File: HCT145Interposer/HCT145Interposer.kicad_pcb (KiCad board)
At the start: 2 copper layers, 33 x 40.6 mm, 8 parts, among them J1 Conn_01x01, J3 Header, J7 FORWARD, J8 REVERSE, U1 74HCT125, U2 74LVC245

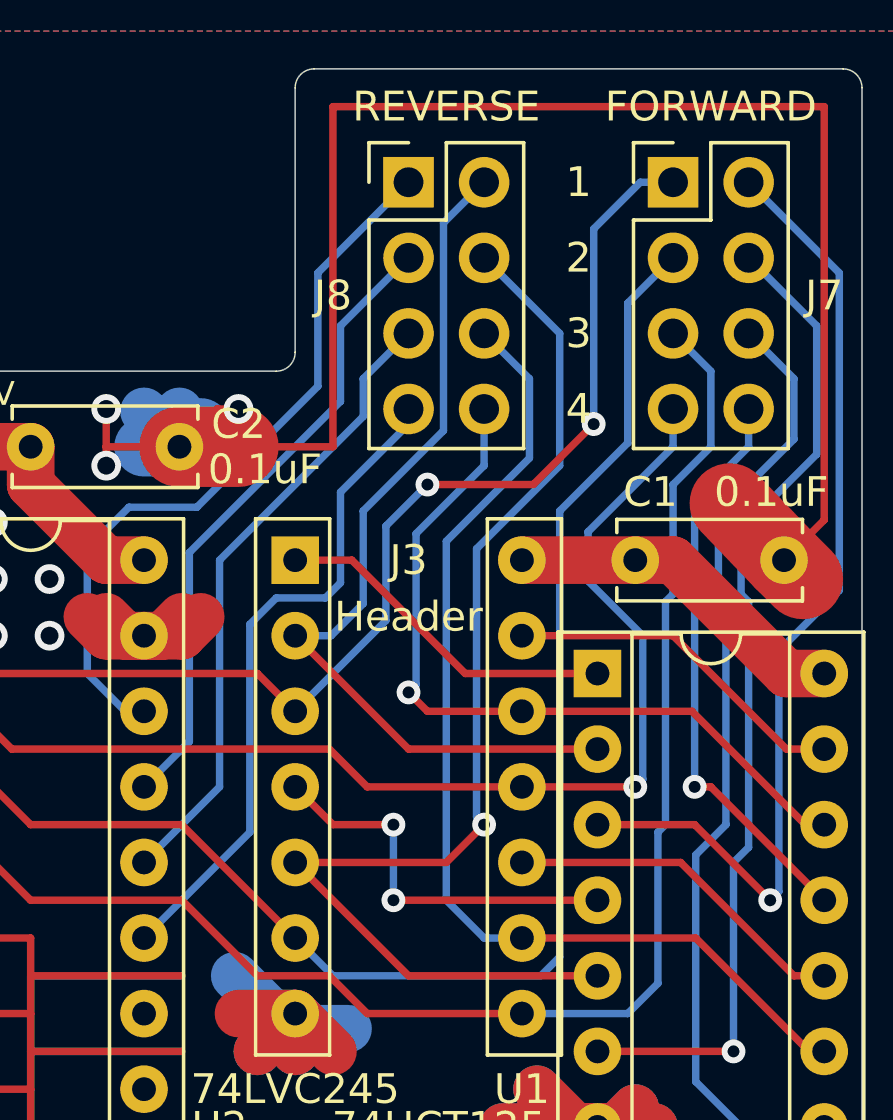
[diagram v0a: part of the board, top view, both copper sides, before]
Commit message: Quick fix to HCT145 interposer. Reverse direction was outputting to wrong pins.
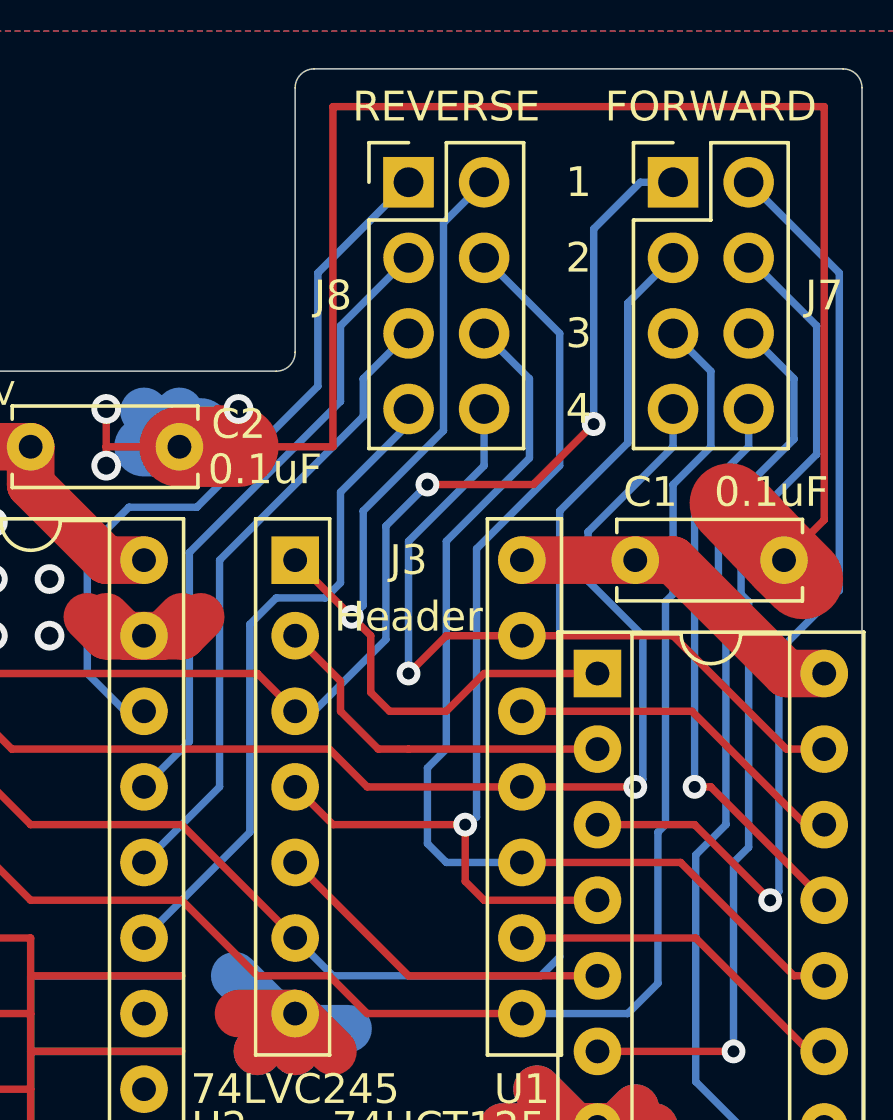
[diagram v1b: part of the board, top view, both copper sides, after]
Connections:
- J8 pad 2: GATE0_IN -> GATE0_~OE
- J8 pad 4: GATE1_IN -> GATE1_~OE
- J8 pad 6: GATE2_IN -> GATE2_~OE
- J8 pad 8: GATE3_IN -> GATE3_~OE
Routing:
- net GATE1_IN: track 40.0 -> 11.7 mm, vias 1 -> 0
- net GATE2_IN: track 35.6 -> 11.7 mm
- net GATE2_~OE: track 11.7 -> 34.4 mm
- net GATE1_~OE: track 13.2 -> 34.3 mm, vias 2 -> 1
- net GATE0_~OE: track 11.7 -> 30.4 mm, vias 0 -> 1
- net GATE0_IN: track 30.3 -> 12.3 mm
- net GATE3_IN: track 26.4 -> 11.7 mm, vias 1 -> 0
- net GATE3_~OE: track 11.7 -> 26.0 mm, vias 0 -> 1

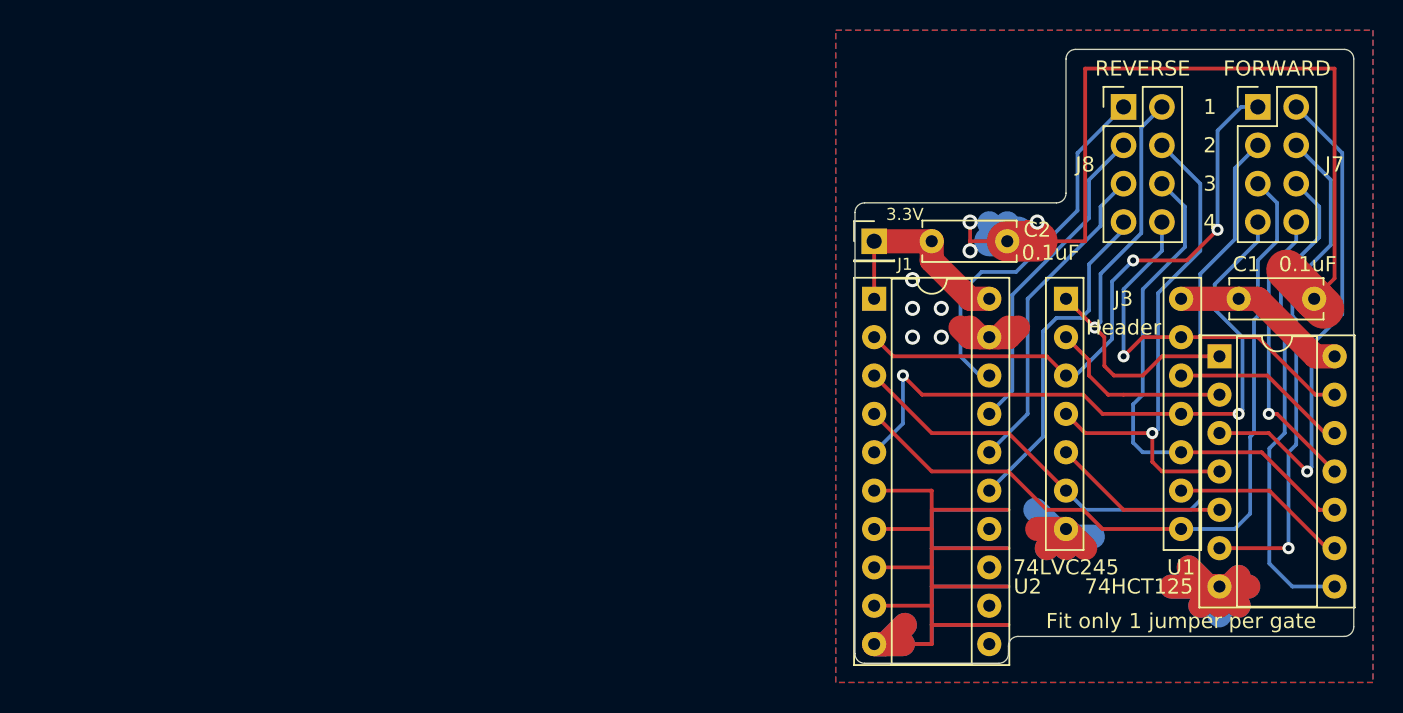
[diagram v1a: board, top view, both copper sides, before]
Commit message: Udate HCT145 interposer. Much simplified (removes the HCT145) and laid out for planning breadboard construction.
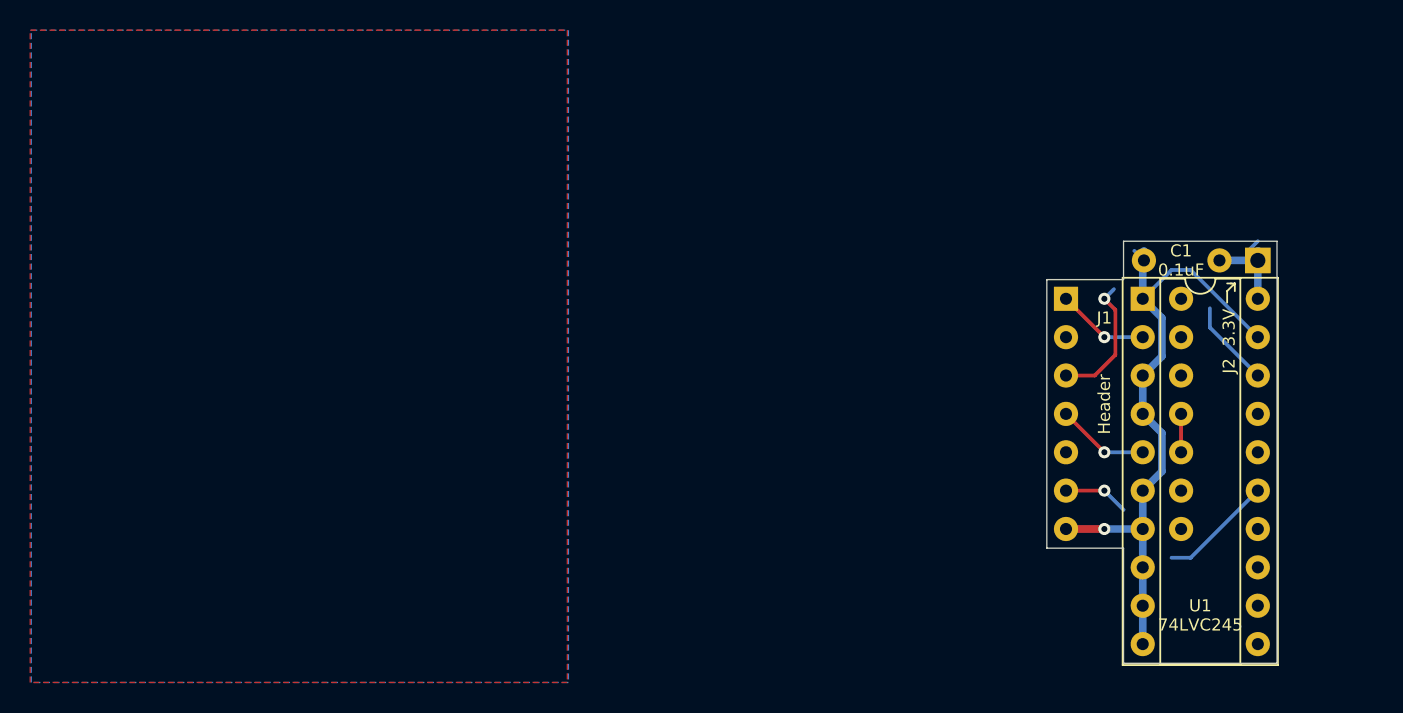
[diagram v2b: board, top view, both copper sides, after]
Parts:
- removed C2: 0.1uF, Capacitor_THT:C_Disc_D6.0mm_W2.5mm_P5.00mm
- removed J7: FORWARD, Connector_PinHeader_2.54mm:PinHeader_2x04_P2.54mm_Vertical
- removed J8: REVERSE, Connector_PinHeader_2.54mm:PinHeader_2x04_P2.54mm_Vertical
- removed the U1 at (124.5, 97.8)
- moved J2 25.4 mm to (127.0, 91.4)
- moved U1 17.8 mm to (119.4, 94.0)
- moved C1 2.84 mm to (124.5, 91.4), turned to 180 degrees
- renumbered J3 to J1, J1 to J2, U2 to U1
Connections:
- C1 pad 1: +5V -> +3V3
- J1 pad 1: GATE0_~OE -> NEW_DRQ_OUT_3V3
- J1 pad 10: GATE2_~OE -> /~DRIVE_ACTIVE~_IN_3V3_1
- J1 pad 11: GATE3_OUT -> /~DRIVE_ACTIVE~_IN_3V3_1
- J1 pad 12: GATE3_IN -> /TIED_TO_GND_2
- J1 pad 13: GATE3_~OE -> /~DRIVE_ACTIVE~_IN_3V3_2
- J1 pad 2: GATE0_IN -> /TIED_TO_5V_1
- J1 pad 3: GATE0_OUT -> NEW_DRQ_IN
- J1 pad 4: GATE1_~OE -> NEW_IRQ_OUT_3V3
- J1 pad 5: GATE1_IN -> /TIED_TO_5V_2
- J1 pad 6: GATE1_OUT -> NEW_IRQ_IN
- J1 pad 8: GATE2_OUT -> /~DRIVE_ACTIVE
- J1 pad 9: GATE2_IN -> /TIED_TO_GND_1
- U1 pad 1: +3V3 -> GND
- U1 pad 15: GATE3_245_OUT -> NEW_IRQ_IN
- U1 pad 16: GATE2_245_OUT -> Net-(U1-Pad16)
- U1 pad 17: GATE1_245_OUT -> Net-(U1-Pad17)
- U1 pad 18: GATE0_245_OUT -> NEW_DRQ_IN
- U1 pad 2: GATE0_OUT -> NEW_DRQ_OUT_3V3
- U1 pad 3: GATE1_OUT -> GND
- U1 pad 4: GATE2_OUT -> GND
- U1 pad 5: GATE3_OUT -> NEW_IRQ_OUT_3V3
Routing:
- net GND: track 203.6 -> 44.3 mm, vias 8 -> 1
- net GATE2_OUT: track 51.6 -> 0.00 mm
- net GATE1_OUT: track 50.6 -> 0.00 mm
- net GATE3_OUT: track 43.9 -> 0.00 mm, vias 2 -> 0
- net GATE0_OUT: track 39.9 -> 0.00 mm, vias 2 -> 0
- net GATE2_~OE: track 34.4 -> 0.00 mm
- net GATE1_~OE: track 34.3 -> 0.00 mm, vias 1 -> 0
- net GATE1_125_OUT: track 33.6 -> 0.00 mm, vias 1 -> 0
- net GATE0_125_OUT: track 33.2 -> 0.00 mm, vias 1 -> 0
- net GATE2_125_OUT: track 32.3 -> 0.00 mm
- net GATE0_~OE: track 30.4 -> 0.00 mm, vias 1 -> 0
- net GATE3_~OE: track 26.0 -> 0.00 mm, vias 1 -> 0
- net GATE0_245_OUT: track 24.8 -> 0.00 mm
- net GATE3_245_OUT: track 22.4 -> 0.00 mm
- net GATE1_245_OUT: track 21.5 -> 0.00 mm
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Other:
- board size 33 x 40.6 mm -> 15.2 x 27.9 mm
- board text removed: "1"
- board text removed: "2"
- board text removed: "3"
- board text removed: "4"
- board text removed: "Fit only 1 jumper per gate"
